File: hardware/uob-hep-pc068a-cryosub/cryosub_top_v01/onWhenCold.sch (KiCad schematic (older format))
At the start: 19 parts, among them Q4 BSS127S, Q5 BSS127S, Q6 FDD306P

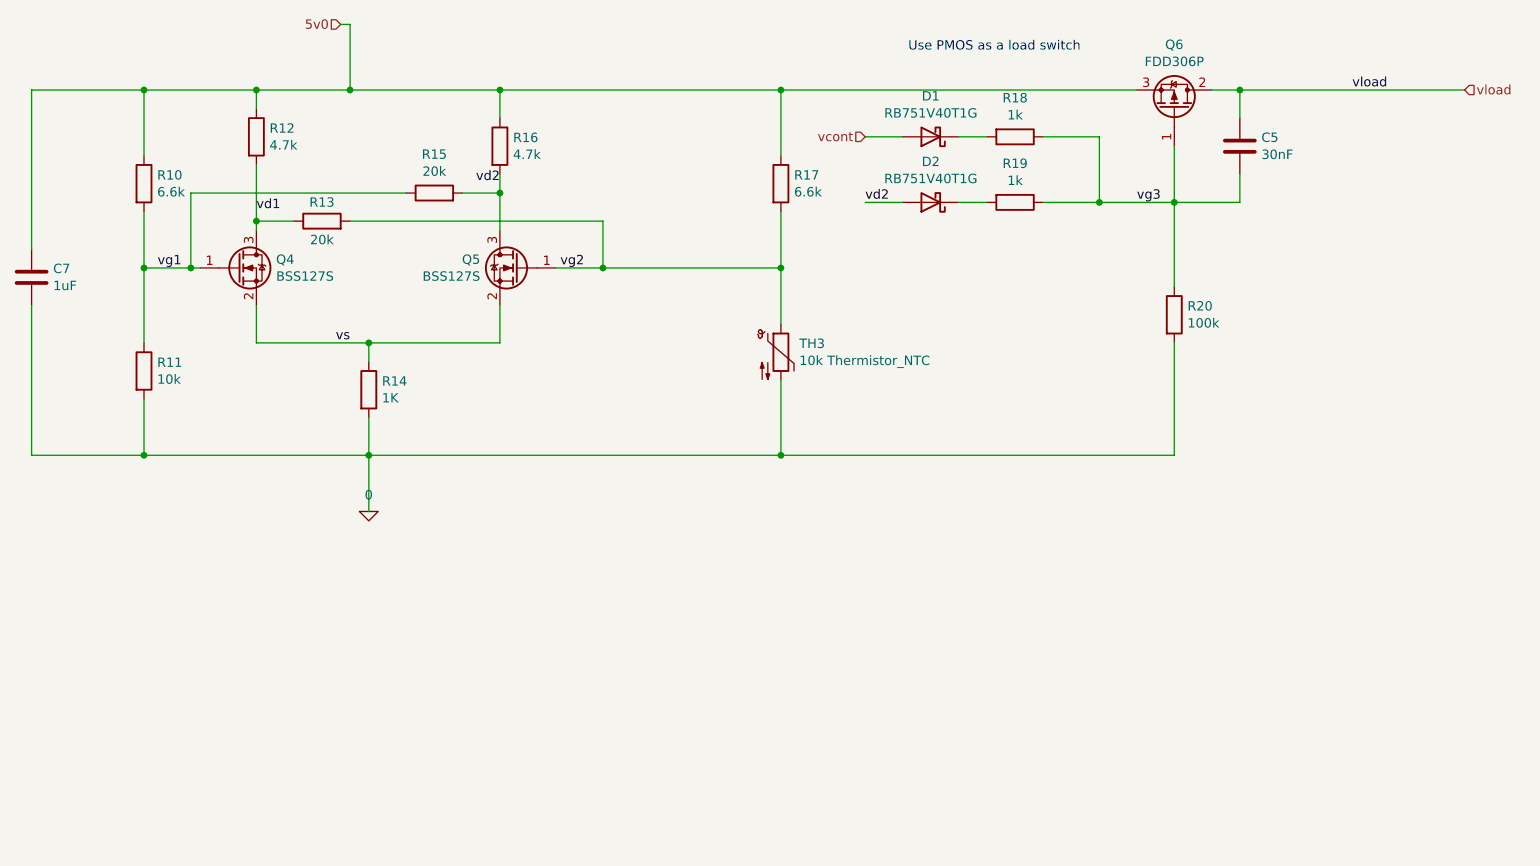
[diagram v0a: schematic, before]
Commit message: Tuning simulation to change on/off temperature. Then making the resulting changes to BoM
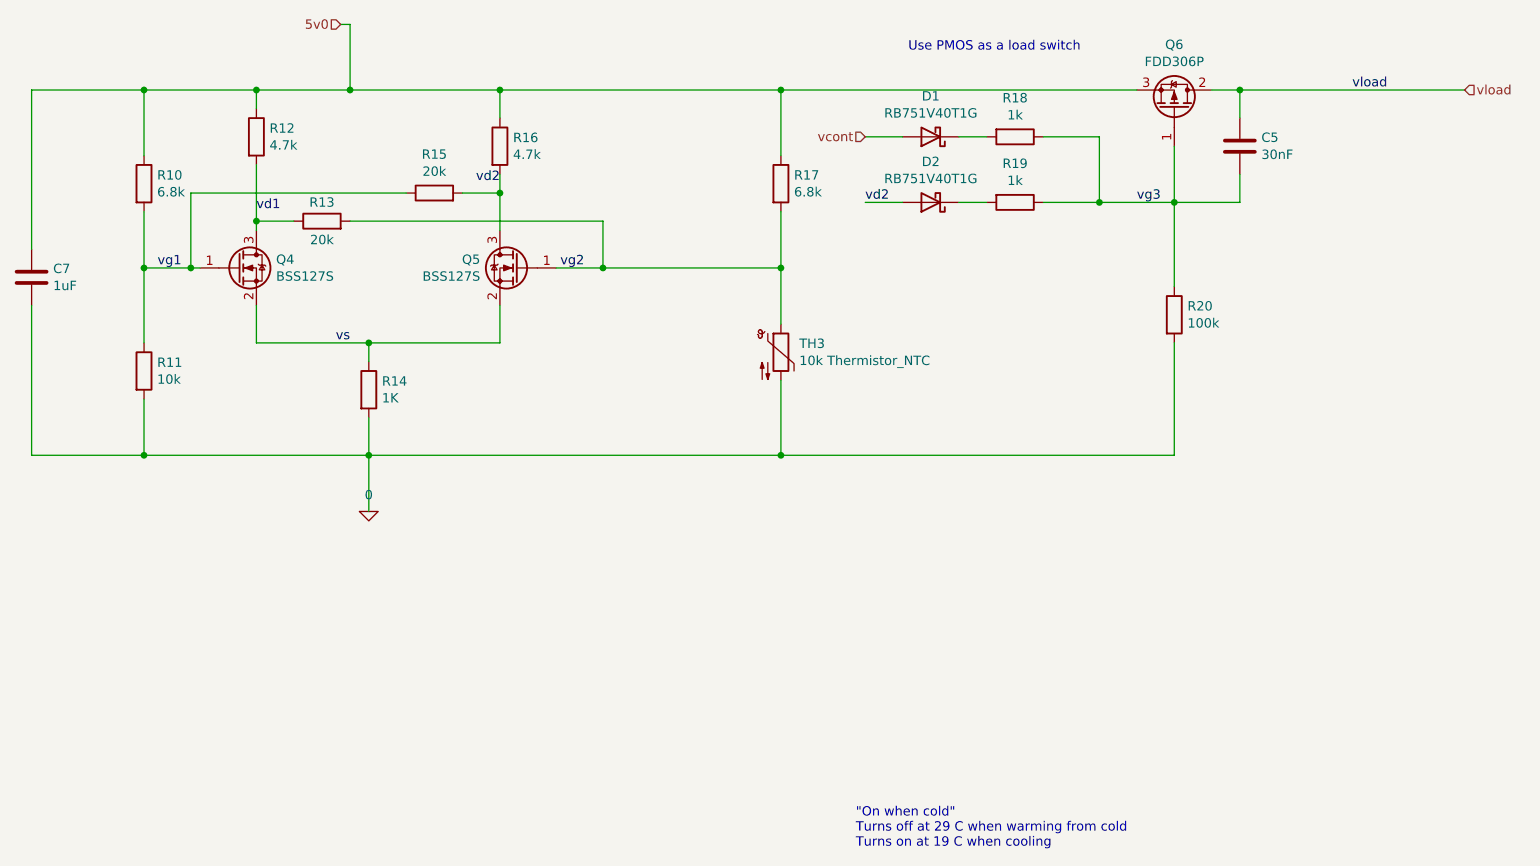
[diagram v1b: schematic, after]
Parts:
- R10, R17: value 6.6k -> 6.8k
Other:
- note added: ""On when cold"\nTurns off at 29 C when warming from cold\nTurns on at 19 C when cooling"
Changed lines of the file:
@@
 P 6750 3400
 F 0 "R17" H 6820 3445 50  0000 L CNN
-F 1 "6.6k" H 6820 3355 50  0000 L CNN
+F 1 "6.8k" H 6820 3355 50  0000 L CNN
 F 2 "Resistor_SMD:R_0603_1608Metric_Pad0.98x0.95mm_HandSolder" V 6680 3400 50  0001 C CNN
 F 3 "~" H 6750 3400 50  0001 C CNN
@@
 P 3350 3400
 F 0 "R10" H 3420 3445 50  0000 L CNN
-F 1 "6.6k" H 3420 3355 50  0000 L CNN
+F 1 "6.8k" H 3420 3355 50  0000 L CNN
 F 2 "Resistor_SMD:R_0603_1608Metric_Pad0.98x0.95mm_HandSolder" V 3280 3400 50  0001 C CNN
 F 3 "~" H 3350 3400 50  0001 C CNN
@@
 Wire Wire Line
 	2750 4050 2750 4850
+Text Notes 7150 6950 0    50   ~ 0
+"On when cold"\nTurns off at 29 C when warming from cold\nTurns on at 19 C when cooling
 $EndSCHEMATC

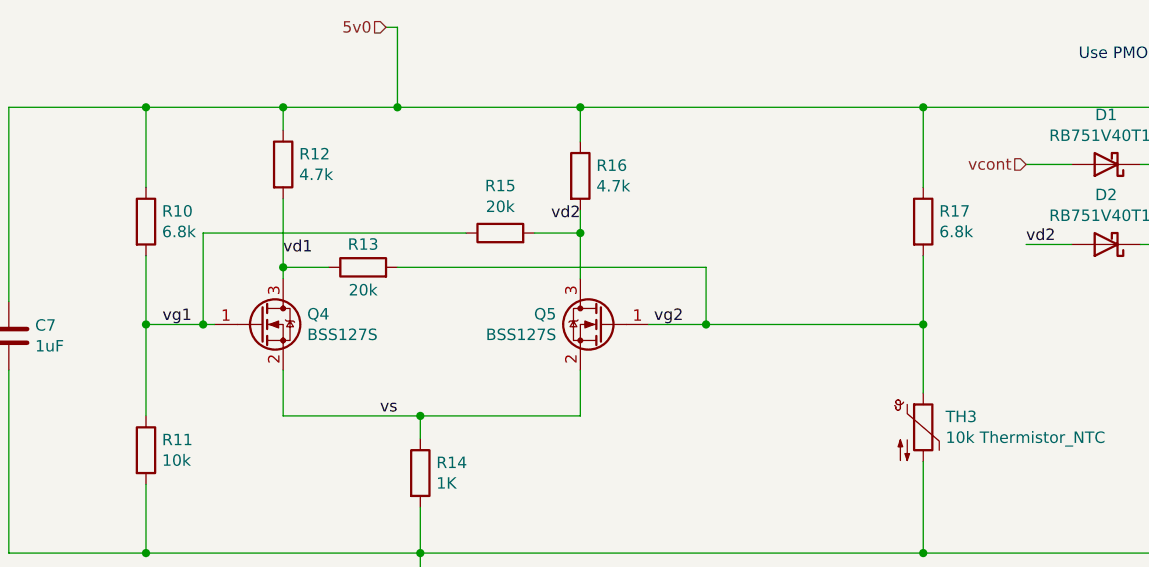
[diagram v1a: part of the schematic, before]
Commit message: Changed mosfet from bss127s --> irlml2402 (which has lower threshold voltage and higher transconductance
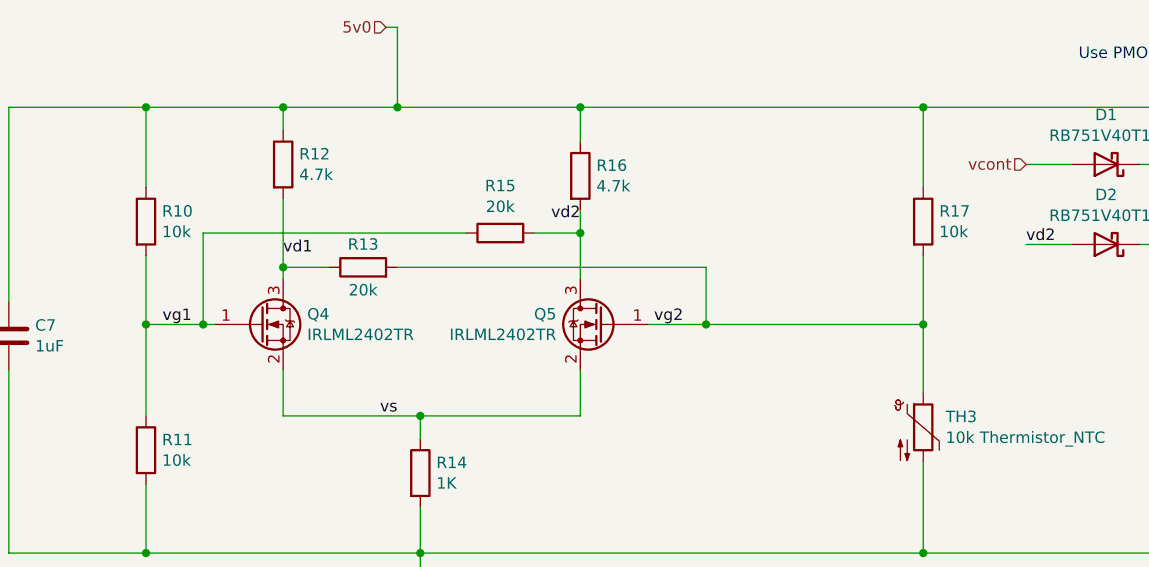
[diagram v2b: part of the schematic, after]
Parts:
- Q4, Q5: value BSS127S -> IRLML2402TR
- R10, R17: value 6.8k -> 10k
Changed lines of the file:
@@
 P 6750 3400
 F 0 "R17" H 6820 3445 50  0000 L CNN
-F 1 "6.8k" H 6820 3355 50  0000 L CNN
+F 1 "10k" H 6820 3355 50  0000 L CNN
 F 2 "Resistor_SMD:R_0603_1608Metric_Pad0.98x0.95mm_HandSolder" V 6680 3400 50  0001 C CNN
 F 3 "~" H 6750 3400 50  0001 C CNN
@@
 P 5350 3850
 F 0 "Q5" H 5555 3895 50  0000 L CNN
-F 1 "BSS127S" H 5555 3805 50  0000 L CNN
+F 1 "IRLML2402TR" H 5555 3805 50  0000 L CNN
 F 2 "Package_TO_SOT_SMD:SOT-23" H 5550 3775 50  0001 L CIN
 F 3 "http://www.diodes.com/assets/Datasheets/BSS127.pdf" H 5350 3850 50  0001 L CNN
@@
 P 3850 3850
 F 0 "Q4" H 4055 3895 50  0000 L CNN
-F 1 "BSS127S" H 4055 3805 50  0000 L CNN
+F 1 "IRLML2402TR" H 4055 3805 50  0000 L CNN
 F 2 "Package_TO_SOT_SMD:SOT-23" H 4050 3775 50  0001 L CIN
 F 3 "http://www.diodes.com/assets/Datasheets/BSS127.pdf" H 3850 3850 50  0001 L CNN
@@
 P 3350 3400
 F 0 "R10" H 3420 3445 50  0000 L CNN
-F 1 "6.8k" H 3420 3355 50  0000 L CNN
+F 1 "10k" H 3420 3355 50  0000 L CNN
 F 2 "Resistor_SMD:R_0603_1608Metric_Pad0.98x0.95mm_HandSolder" V 3280 3400 50  0001 C CNN
 F 3 "~" H 3350 3400 50  0001 C CNN
